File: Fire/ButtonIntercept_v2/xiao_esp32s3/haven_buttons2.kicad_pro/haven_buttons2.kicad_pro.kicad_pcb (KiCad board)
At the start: 2 copper layers, 56 x 92 mm, 47 parts, among them J1 Conn_01x07_Socket, J2 Conn_01x07_Socket, J3 Screw_Terminal_01x04, J4 Screw_Terminal_01x04, J6 Screw_Terminal_01x04, J7 Screw_Terminal_01x04, J8 Screw_Terminal_01x02, J9 Screw_Terminal_01x04, Q1 BC817, Q2 BC817, Q3 BC817, Q4 BC817, Q5 BC817, Q6 BC817, Q7 BC817, Q8 BC817, SW1 SW_DIP_x03, U2 PCA9555PW, U21 TLV1117-50IDCYR

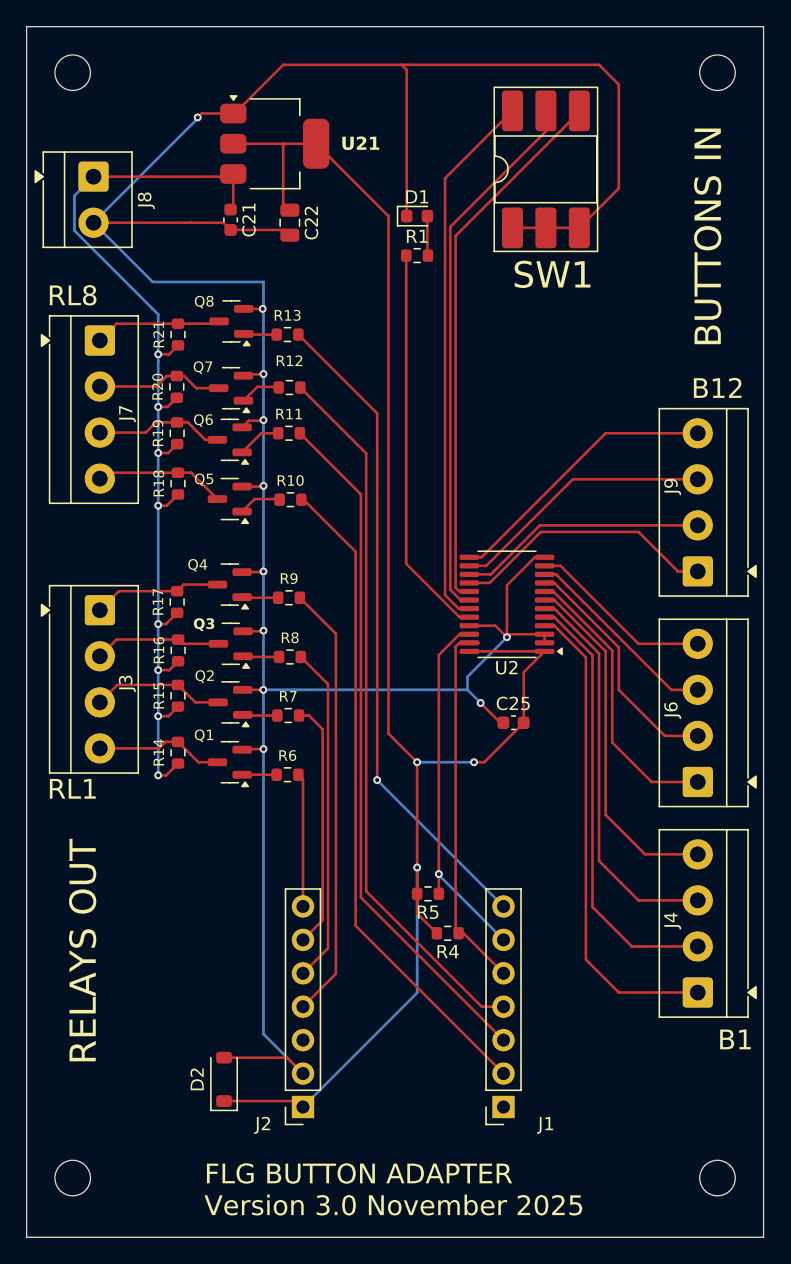
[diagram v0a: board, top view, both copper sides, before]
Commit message: modified board files for button intercept with xiao esp32s3
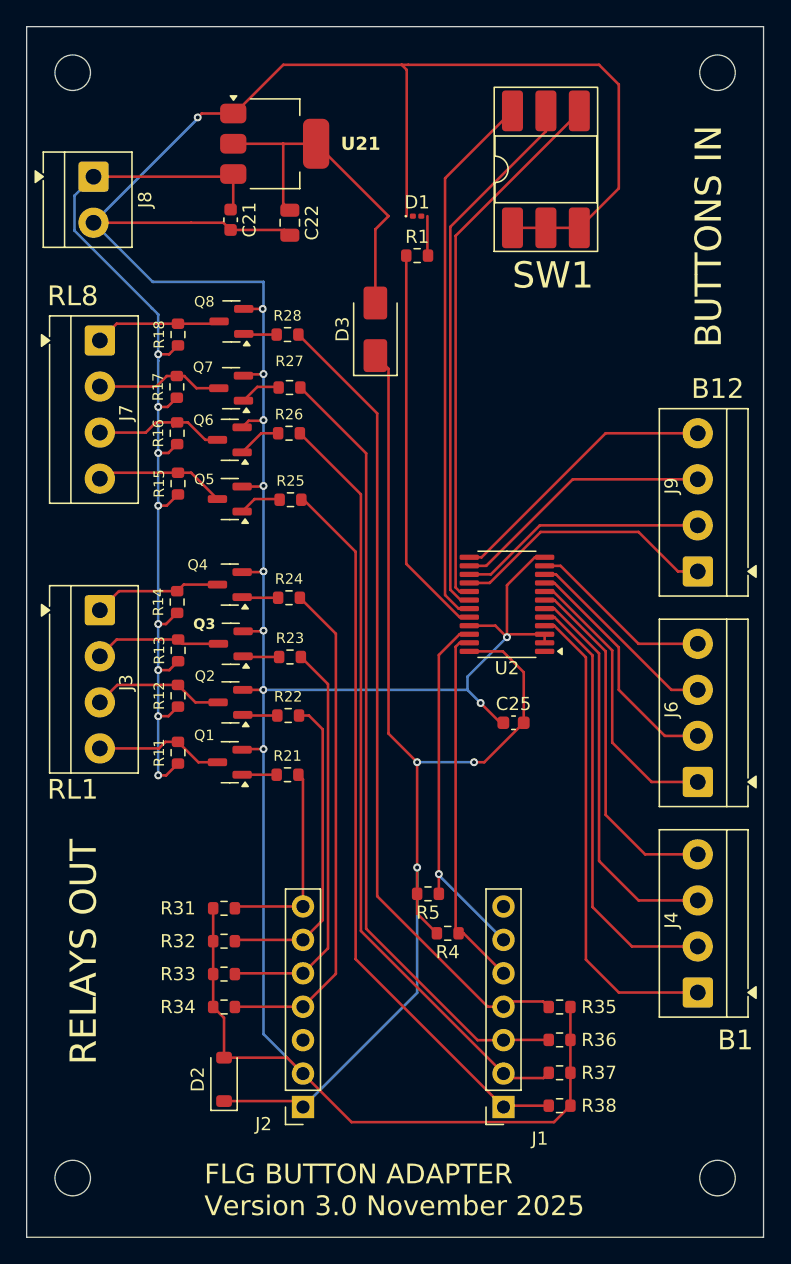
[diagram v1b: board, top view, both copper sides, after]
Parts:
- added D3: US1A, Diode_SMD:D_SMA, F.Cu at (81.0, 67.5)
- added R31: 10k, Resistor_SMD:R_0603_1608Metric, F.Cu at (69.5, 111.5)
- added R32: 10k, Resistor_SMD:R_0603_1608Metric, F.Cu at (69.5, 114.0)
- added R33: 10k, Resistor_SMD:R_0603_1608Metric, F.Cu at (69.5, 116.5)
- added R34: 10k, Resistor_SMD:R_0603_1608Metric, F.Cu at (69.5, 119.0)
- added R35: 10k, Resistor_SMD:R_0603_1608Metric, F.Cu at (95.0, 119.0)
- added R36: 10k, Resistor_SMD:R_0603_1608Metric, F.Cu at (95.0, 121.5)
- added R37: 10k, Resistor_SMD:R_0603_1608Metric, F.Cu at (95.0, 124.0)
- added R38: 10k, Resistor_SMD:R_0603_1608Metric, F.Cu at (95.0, 126.5)
- D1: footprint LED_SMD:LED_0603_1608Metric -> LED_SMD:LED_0201_0603Metric
- renumbered R14 to R11, R15 to R12, R16 to R13, R17 to R14, R18 to R15, R19 to R16, R20 to R17, R21 to R18, R6 to R21, R7 to R22, R8 to R23, R9 to R24, R10 to R25, R11 to R26, R12 to R27, R13 to R28
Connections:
- C22 pad 1: +5V -> Net-(D3-A)
- J1 pad 1: /AUX -> /OUT 8
- J1 pad 2: /OUT 5 -> /OUT 7
- J1 pad 4: /OUT 7 -> /OUT 5
- J1 pad 7: /OUT 8 -> unconnected-(J1-Pin_7-Pad7)
- U2 pad 1: +5V -> unconnected-(U2-~{INT}-Pad1)
- U21 pad 2: +5V -> Net-(D3-A)
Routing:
- net GND: track 223.7 -> 265.3 mm
- net +5V: track 124.5 -> 91.8 mm
- net Net-(D3-A): track 0.00 -> 26.3 mm
- net /OUT 8: track 50.1 -> 61.9 mm, vias 1 -> 0
- net /OUT 6: track 52.5 -> 58.7 mm
- net /OUT 7: track 54.4 -> 60.5 mm
- net /OUT 5: track 50.1 -> 56.0 mm
- net /OUT 1: track 10.2 -> 15.4 mm
- net /OUT 2: track 18.9 -> 24.1 mm
- net /OUT 3: track 25.7 -> 30.9 mm
- net /OUT 4: track 33.2 -> 38.4 mm
- net /SDA: track 28.4 -> 27.7 mm
